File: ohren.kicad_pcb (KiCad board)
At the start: 2 copper layers, 60 x 28.7 mm, 29 parts, among them J1 Conn_01x19_MountingPin, U1 TLC5955RTQ

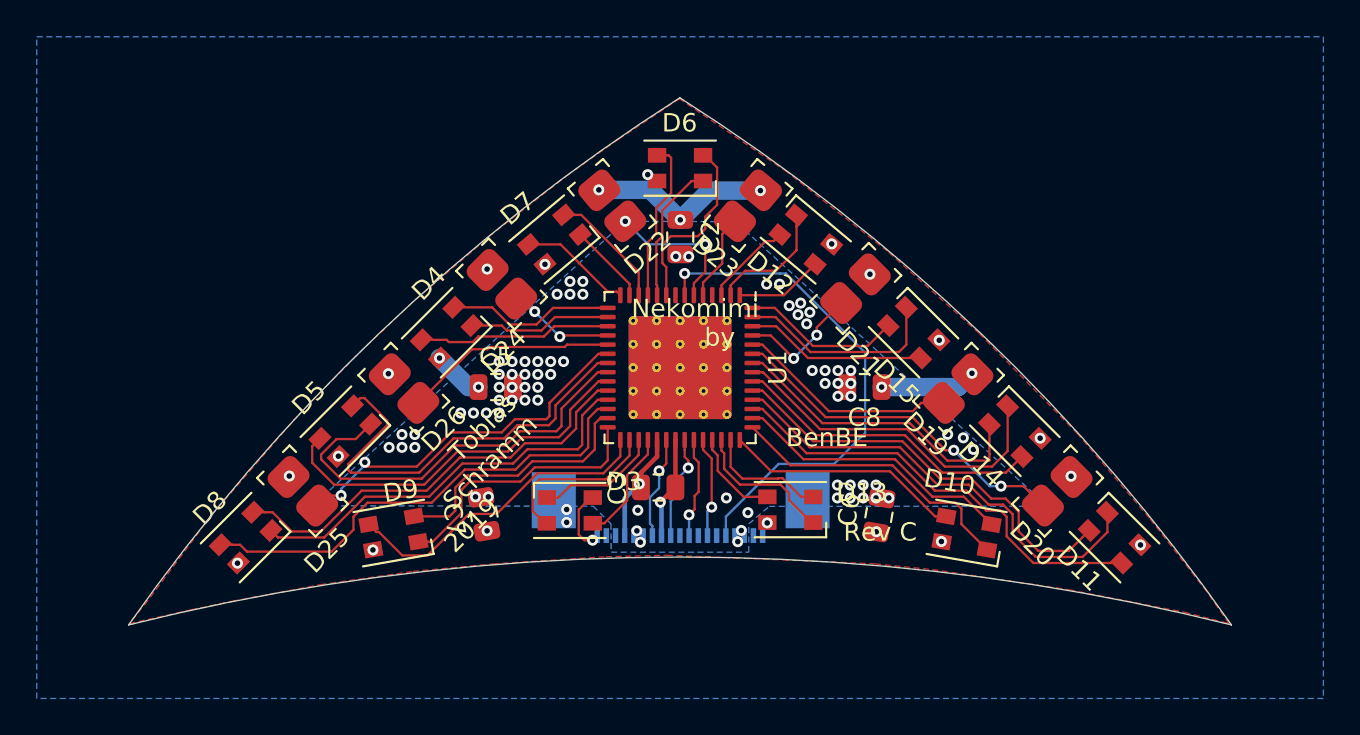
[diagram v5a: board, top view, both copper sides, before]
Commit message: Readjust silkscreen designators
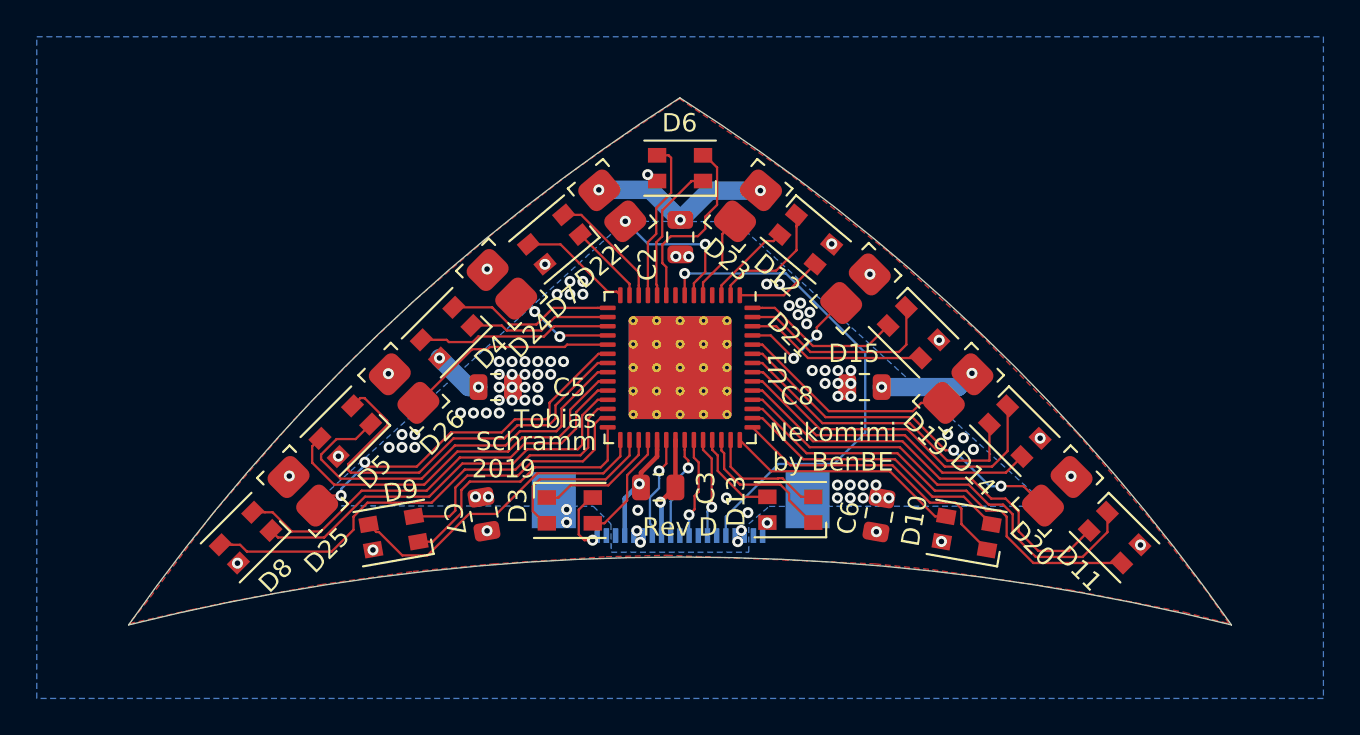
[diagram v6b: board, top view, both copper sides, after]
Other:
- board text added: "Nekomimi by BenBE"
- board text added: "Rev D"
- board text added: "Schramm"
- board text added: "Tobias"
- board text removed: "BenBE"
- board text removed: "Nekomimi"
- board text removed: "Rev C"
- board text removed: "Tobias Schramm"
- board text removed: "by"
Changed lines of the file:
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@@
   (general
     (thickness 1.6)
-    (drawings 16)
+    (drawings 13)
     (tracks 554)
     (zones 0)
@@
   (page A4)
   (layers
-    (0 F.Cu signal)
-    (31 B.Cu signal)
-    (32 B.Adhes user)
-    (33 F.Adhes user)
-    (34 B.Paste user)
+    (0 F.Cu signal hide)
+    (31 B.Cu signal hide)
+    (32 B.Adhes user hide)
+    (33 F.Adhes user hide)
+    (34 B.Paste user hide)
     (35 F.Paste user)
     (36 B.SilkS user)
@@
     (tags capacitor)
     (attr smd)
-    (fp_text reference C5 (at 0 -1.65 180) (layer F.SilkS)
+    (fp_text reference C5 (at 4.01 0.02 180) (layer F.SilkS)
       (effects (font (size 1 1) (thickness 0.15)))
     )
@@
   (module catear-pcb:Molex_Easy-On_52746-1971_1x19_P0.5mm_Horizontal (layer B.Cu)
     (at 139.99 111.14)
-    (fp_text reference J1 (at -15.6 -2.5) (layer B.SilkS)
+    (fp_text reference J1 (at -9.51 -1.49) (layer B.SilkS)
       (effects (font (size 1 1) (thickness 0.15)) (justify mirror))
     )
@@
     (tags capacitor)
     (attr smd)
-    (fp_text reference C8 (at 0 -1.65 180) (layer F.SilkS)
+    (fp_text reference C8 (at 3.66 -0.48 180) (layer F.SilkS)
       (effects (font (size 1 1) (thickness 0.15)))
     )
@@
     (tags capacitor)
     (attr smd)
-    (fp_text reference C6 (at 0.000001 -1.65 260) (layer F.SilkS)
+    (fp_text reference C6 (at -0.437714 -1.618582 260) (layer F.SilkS)
       (effects (font (size 1 1) (thickness 0.15)))
     )
@@
     (tags capacitor)
     (attr smd)
-    (fp_text reference C2 (at 0 -1.65 270) (layer F.SilkS)
+    (fp_text reference C2 (at 1.48 1.79 270) (layer F.SilkS)
       (effects (font (size 1 1) (thickness 0.15)))
     )
@@
   (module catear-pcb:smd_led_universal (layer F.Cu)
     (at 149.56 97.69 45)
-    (fp_text reference D21 (at -2.390021 2.644579 135) (layer F.SilkS)
+    (fp_text reference D21 (at -4.320422 -0.742462 135) (layer F.SilkS)
       (effects (font (size 1 1) (thickness 0.15)))
     )
@@
     (tags "LED Cree PLCC-4")
     (attr smd)
-    (fp_text reference D3 (at 2.96 -1.57) (layer F.SilkS)
+    (fp_text reference D3 (at -2.83 -0.25 90) (layer F.SilkS)
       (effects (font (size 1 1) (thickness 0.15)))
     )
@@
     (tags "LED Cree PLCC-4")
     (attr smd)
-    (fp_text reference D13 (at -3.895 0.935) (layer F.SilkS)
+    (fp_text reference D13 (at 2.96 0.46 90) (layer F.SilkS)
       (effects (font (size 1 1) (thickness 0.15)))
     )
@@
   (module catear-pcb:smd_led_universal (layer F.Cu)
     (at 124.968 103.124 135)
-    (fp_text reference D26 (at -3.116927 -0.016971 225) (layer F.SilkS)
+    (fp_text reference D26 (at -3.194708 -0.222032 225) (layer F.SilkS)
       (effects (font (size 1 1) (thickness 0.15)))
     )
@@
   (module catear-pcb:smd_led_universal (layer F.Cu)
     (at 130.29 97.45 135)
-    (fp_text reference D24 (at -2.662257 -2.499622 225) (layer F.SilkS)
+    (fp_text reference D24 (at -3.125412 -0.834386 225) (layer F.SilkS)
       (effects (font (size 1 1) (thickness 0.15)))
     )
@@
   (module catear-pcb:smd_led_universal (layer F.Cu)
     (at 143.71 93.1782 50)
-    (fp_text reference D23 (at -3.286019 0.427145 140) (layer F.SilkS)
+    (fp_text reference D23 (at -3.000416 1.016429 140) (layer F.SilkS)
       (effects (font (size 1 1) (thickness 0.15)))
     )
@@
   (module catear-pcb:smd_led_universal (layer F.Cu)
     (at 136.296864 93.1782 130)
-    (fp_text reference D22 (at -3.211476 -0.158165 220) (layer F.SilkS)
+    (fp_text reference D22 (at -2.072232 -2.713771 220) (layer F.SilkS)
       (effects (font (size 1 1) (thickness 0.15)))
     )
@@
     (tags capacitor)
     (attr smd)
-    (fp_text reference C3 (at -2.22 0.05 90) (layer F.SilkS)
+    (fp_text reference C3 (at 2.59 0.03 90) (layer F.SilkS)
       (effects (font (size 1 1) (thickness 0.15)))
     )
@@
     (tags "LED Cree PLCC-4")
     (attr smd)
-    (fp_text reference D15 (at 1.233901 2.542049 315) (layer F.SilkS)
+    (fp_text reference D15 (at -1.484924 3.082986) (layer F.SilkS)
       (effects (font (size 1 1) (thickness 0.15)))
     )
@@
     (tags "LED Cree PLCC-4")
     (attr smd)
-    (fp_text reference D14 (at -0.029863 2.580904 315) (layer F.SilkS)
+    (fp_text reference D14 (at 0.033776 3.245584 315) (layer F.SilkS)
       (effects (font (size 1 1) (thickness 0.15)))
     )
@@
     (tags "LED Cree PLCC-4")
     (attr smd)
-    (fp_text reference D12 (at -0.295737 2.650102 320) (layer F.SilkS)
+    (fp_text reference D12 (at 0.072495 2.497768 320) (layer F.SilkS)
       (effects (font (size 1 1) (thickness 0.15)))
     )
@@
     (tags "LED Cree PLCC-4")
     (attr smd)
-    (fp_text reference D10 (at 1.397745 2.571349 350) (layer F.SilkS)
+    (fp_text reference D10 (at 2.913198 0.16666 80) (layer F.SilkS)
       (effects (font (size 1 1) (thickness 0.15)))
     )
@@
     (tags "LED Cree PLCC-4")
     (attr smd)
-    (fp_text reference D8 (at 0.226274 2.5173 225) (layer F.SilkS)
+    (fp_text reference D8 (at 0.297756 -2.615524 225) (layer F.SilkS)
       (effects (font (size 1 1) (thickness 0.15)))
     )
@@
     (tags "LED Cree PLCC-4")
     (attr smd)
-    (fp_text reference D7 (at 0.445778 2.58019 40) (layer F.SilkS)
+    (fp_text reference D7 (at 1.774279 -2.92348 40) (layer F.SilkS)
       (effects (font (size 1 1) (thickness 0.15)))
     )
@@
     (tags "LED Cree PLCC-4")
     (attr smd)
-    (fp_text reference D5 (at 0.114716 2.68697 225) (layer F.SilkS)
+    (fp_text reference D5 (at 0.429756 -2.694041 225) (layer F.SilkS)
       (effects (font (size 1 1) (thickness 0.15)))
     )
@@
     (tags "LED Cree PLCC-4")
     (attr smd)
-    (fp_text reference D4 (at -1.216224 2.588011 45) (layer F.SilkS)
+    (fp_text reference D4 (at -0.968736 -2.467803 45) (layer F.SilkS)
       (effects (font (size 1 1) (thickness 0.15)))
     )
@@
     )
   )
-  (dimension 4.755 (width 0.12) (layer Eco2.User)
-    (gr_text "4,755 mm" (at 186.085 109.5725 90) (layer Eco2.User)
-      (effects (font (size 1 1) (thickness 0.15)))
-    )
-    (feature1 (pts (xy 143.67 107.195) (xy 185.401421 107.195)))
-    (feature2 (pts (xy 143.67 111.95) (xy 185.401421 111.95)))
-    (crossbar (pts (xy 184.815 111.95) (xy 184.815 107.195)))
-    (arrow1a (pts (xy 184.815 107.195) (xy 185.401421 108.321504)))
-    (arrow1b (pts (xy 184.815 107.195) (xy 184.228579 108.321504)))
-    (arrow2a (pts (xy 184.815 111.95) (xy 185.401421 110.823496)))
-    (arrow2b (pts (xy 184.815 111.95) (xy 184.228579 110.823496)))
-  )
-  (dimension 14.32 (width 0.12) (layer Eco2.User)
-    (gr_text "14,320 mm" (at 140 136.495) (layer Eco2.User)
-      (effects (font (size 1 1) (thickness 0.15)))
-    )
-    (feature1 (pts (xy 147.16 110.895) (xy 147.16 135.811421)))
-    (feature2 (pts (xy 132.84 110.895) (xy 132.84 135.811421)))
-    (crossbar (pts (xy 132.84 135.225) (xy 147.16 135.225)))
-    (arrow1a (pts (xy 147.16 135.225) (xy 146.033496 135.811421)))
-    (arrow1b (pts (xy 147.16 135.225) (xy 146.033496 134.638579)))
-    (arrow2a (pts (xy 132.84 135.225) (xy 133.966504 135.811421)))
-    (arrow2b (pts (xy 132.84 135.225) (xy 133.966504 134.638579)))
-  )
-  (dimension 3.12 (width 0.12) (layer Eco2.User)
-    (gr_text "3,120 mm" (at 178.41 109.55 90) (layer Eco2.User)
-      (effects (font (size 1 1) (thickness 0.15)))
-    )
-    (feature1 (pts (xy 147.065 107.99) (xy 177.726421 107.99)))
-    (feature2 (pts (xy 147.065 111.11) (xy 177.726421 111.11)))
-    (crossbar (pts (xy 177.14 111.11) (xy 177.14 107.99)))
-    (arrow1a (pts (xy 177.14 107.99) (xy 177.726421 109.116504)))
-    (arrow1b (pts (xy 177.14 107.99) (xy 176.553579 109.116504)))
-    (arrow2a (pts (xy 177.14 111.11) (xy 177.726421 109.983496)))
-    (arrow2b (pts (xy 177.14 111.11) (xy 176.553579 109.983496)))
-  )
-  (gr_text 2019 (at 128.645 110.57 45) (layer F.SilkS)
+  (gr_poly (pts (xy 137 99) (xy 143 99) (xy 143 105) (xy 137 105)) (layer B.Mask) (width 0.1))
+  (gr_text Schramm (at 135.45 106.02) (layer F.SilkS)
+    (effects (font (size 1 1) (thickness 0.15)) (justify right))
+  )
+  (gr_text 2019 (at 130.41 107.51) (layer F.SilkS)
     (effects (font (size 1 1) (thickness 0.15)))
   )
-  (gr_text "Rev C" (at 150.89 110.95) (layer F.SilkS)
+  (gr_text "Rev D" (at 140 110.68) (layer F.SilkS)
     (effects (font (size 1 1) (thickness 0.15)))
   )
-  (gr_text "Tobias\nSchramm" (at 131.41 104.27 45) (layer F.SilkS)
+  (gr_text Tobias (at 135.44 104.81) (layer F.SilkS)
     (effects (font (size 1 1) (thickness 0.15)) (justify right))
   )
-  (gr_text BenBE (at 147.99 105.81) (layer F.SilkS)
+  (gr_text "Nekomimi\nby BenBE" (at 148.32 106.33) (layer F.SilkS)
     (effects (font (size 1 1) (thickness 0.15)))
   )
-  (gr_text "by\n" (at 142.16 100.35) (layer F.SilkS)
-    (effects (font (size 1 1) (thickness 0.15)))
-  )
-  (gr_text Nekomimi (at 140.82 98.79) (layer F.SilkS)
-    (effects (font (size 1 1) (thickness 0.15)))
-  )
